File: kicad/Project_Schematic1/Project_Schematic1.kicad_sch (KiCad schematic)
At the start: 40 parts, among them M1 Flag_Servo, M2 Motor_Left, M3 Motor_Bottom, M4 Motor_Right, Q1 NPN, Q2 NPN, Q3 NPN, U1 74xxx244, U2 PIC32MX170F256B, U3 CD4052, U4 QTR-HD-01A, U5 Left_Drum_LEDs, U6 Bottom_Drum_LEDs, U7 Right_Drum_LEDs

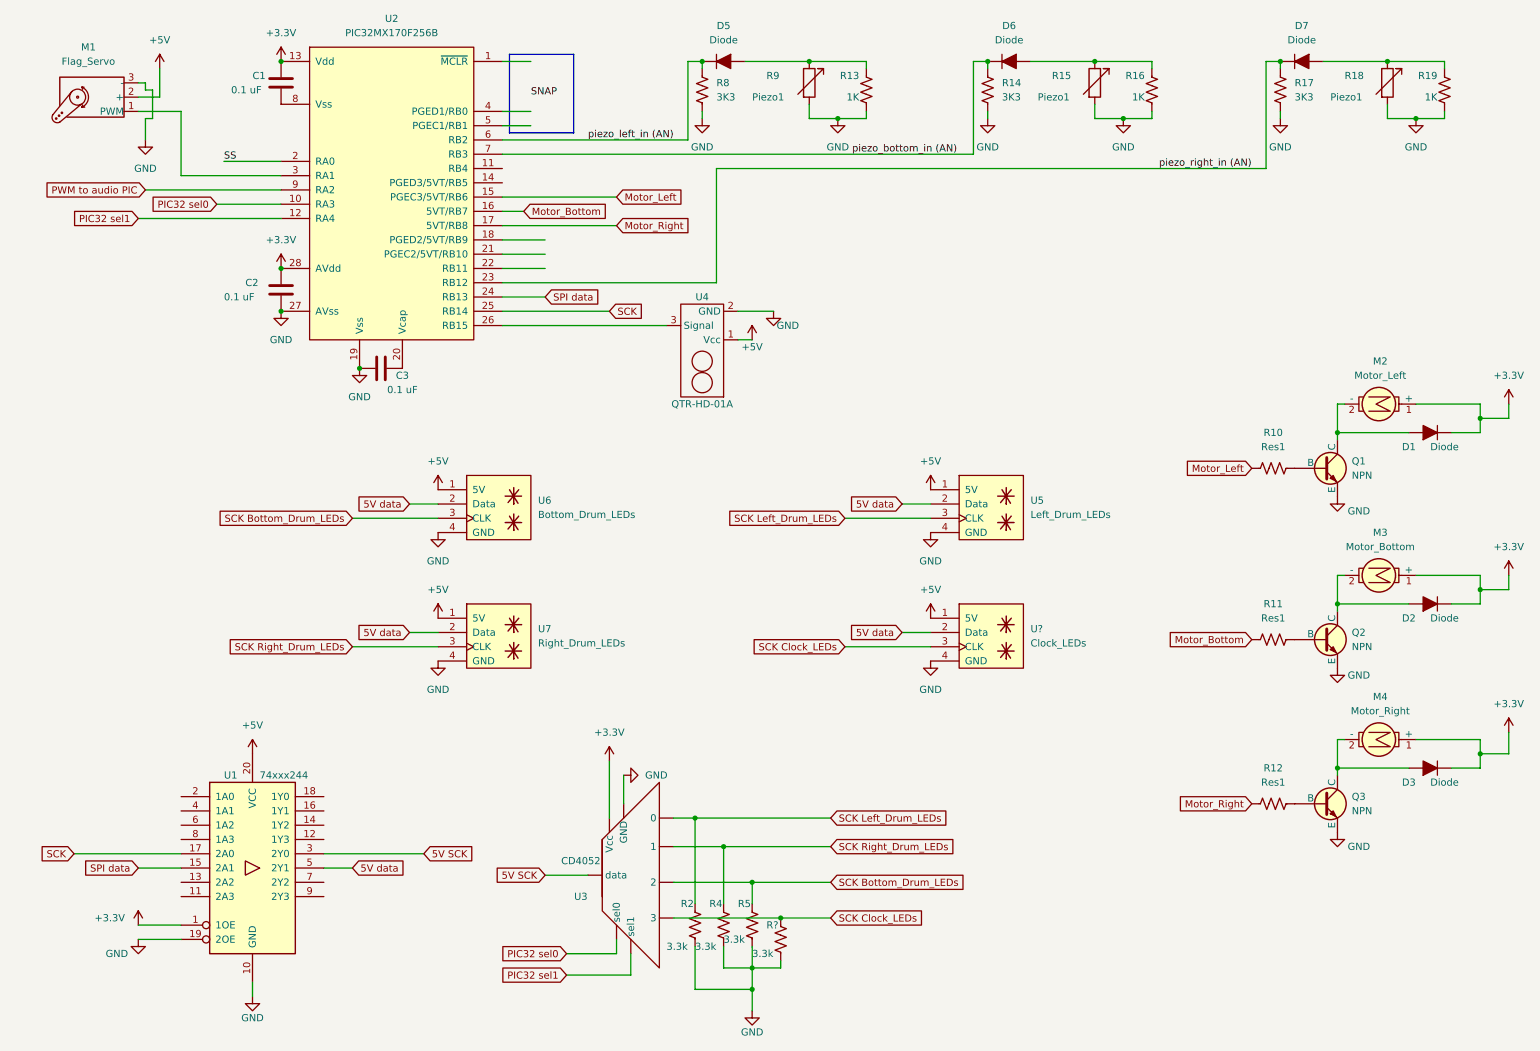
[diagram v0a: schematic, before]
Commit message: Choose custom resistors to constrain piezo voltage below 3.3V
* Rarely exceeds, but especially bottom drum does, so maybe add unity gain buffer
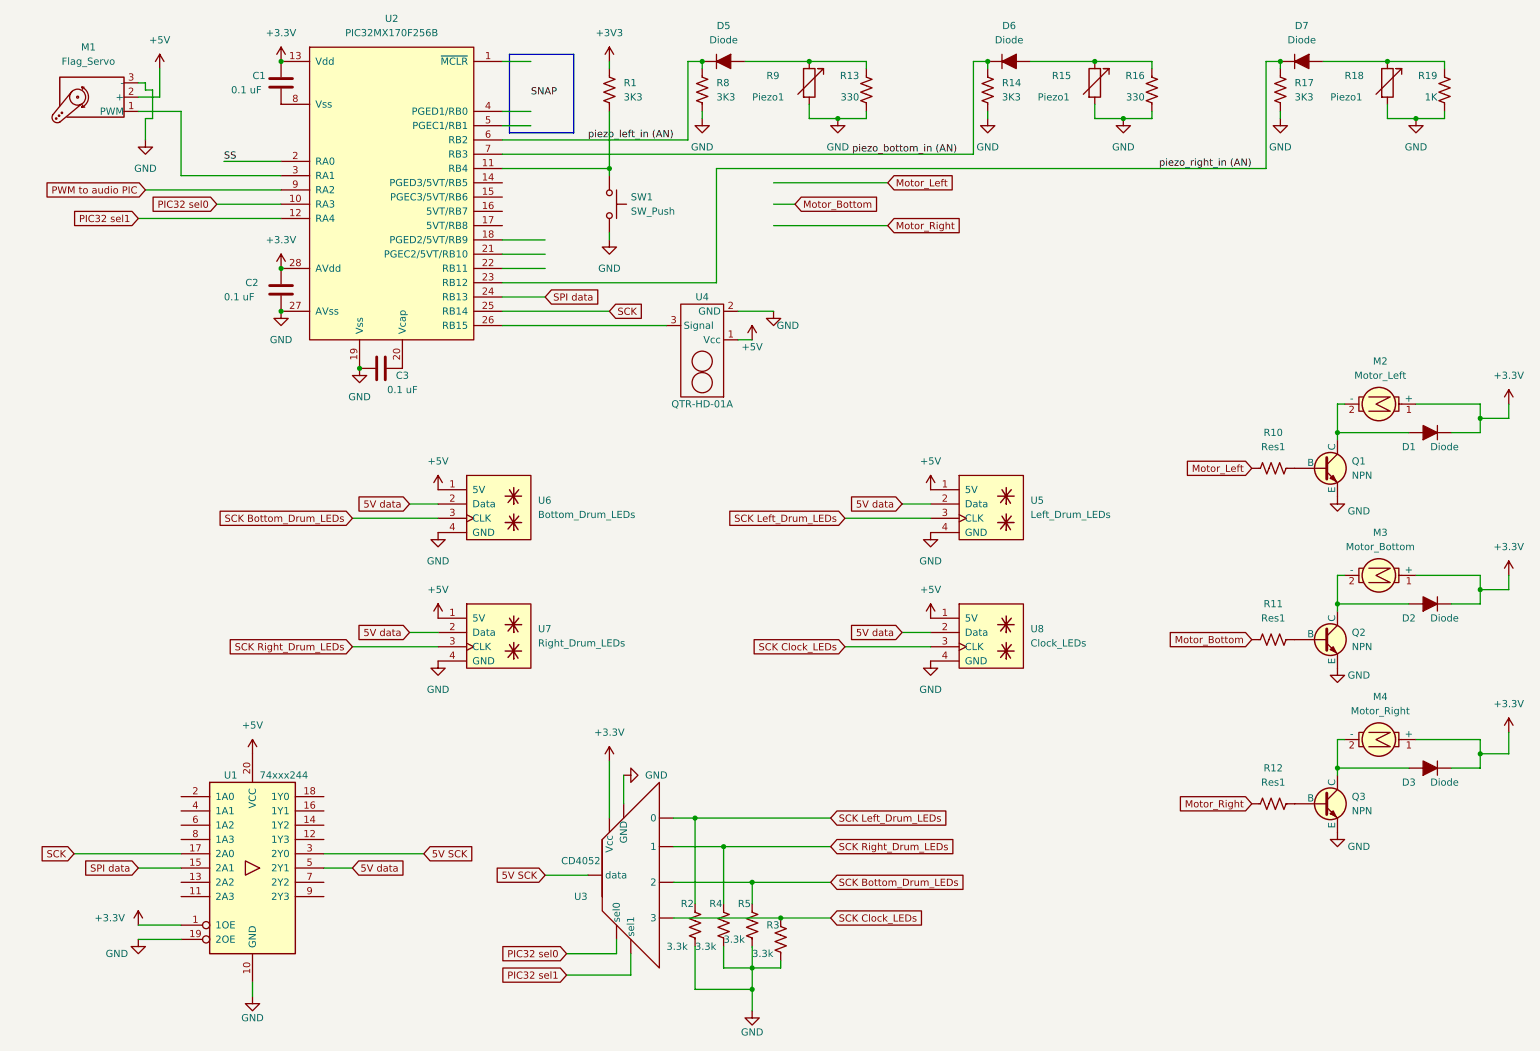
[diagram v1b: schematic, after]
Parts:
- added R1: 3K3, symbol Device:R_US
- added SW1: SW_Push, symbol Switch:SW_Push
- R13, R16: value 1K -> 330
- gave numbers to parts that had none: 2
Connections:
- net GND: now also SW1.2
- net Motor_Bottom: no longer U2.16 (5VT/RB7)
- net Motor_Left: no longer U2.15 (PGEC3/5VT/RB6)
- net Motor_Right: no longer U2.17 (5VT/RB8)
- net at U2.11 (RB4): now also R1.2, SW1.1
- new net +3V3: R1.1

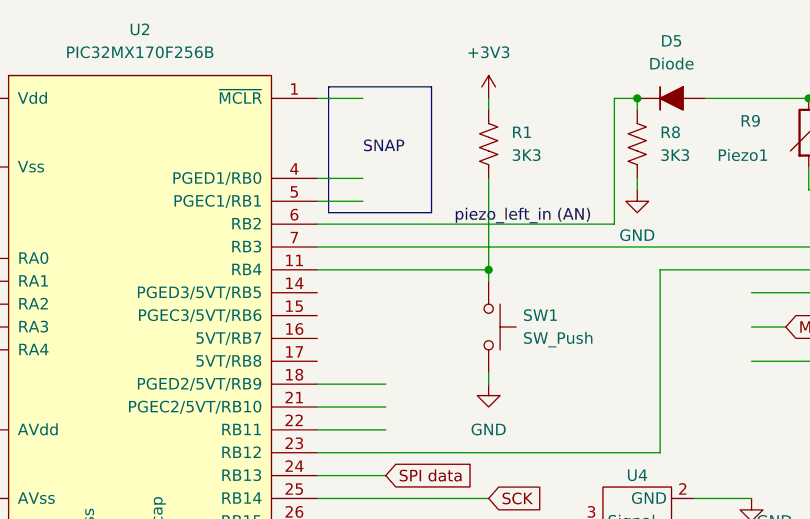
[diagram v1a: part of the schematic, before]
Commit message: Press button to cycle between minimum piezo thresholds
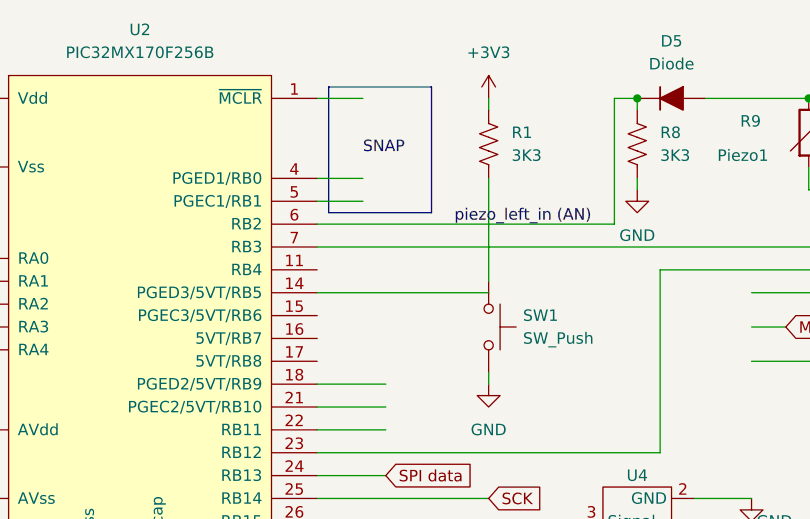
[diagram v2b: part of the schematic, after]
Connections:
- net at R1.2, SW1.1: no longer U2.11 (RB4)
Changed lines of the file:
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@@
   (junction (at 140.97 184.15) (diameter 0) (color 0 0 0 0)
   )
-  (junction (at 115.57 41.91) (diameter 0) (color 0 0 0 0)
-  )
   (junction (at 132.08 22.86) (diameter 0) (color 0 0 0 0)
   )
@@
     (stroke (width 0) (type default) (color 0 0 0 0))
   )
-  (wire (pts (xy 115.57 31.75) (xy 115.57 41.91))
+  (wire (pts (xy 115.57 31.75) (xy 115.57 43.18))
     (stroke (width 0) (type default) (color 0 0 0 0))
   )
@@
     (stroke (width 0) (type default) (color 0 0 0 0))
   )
-  (wire (pts (xy 115.57 41.91) (xy 115.57 43.18))
-    (stroke (width 0) (type default) (color 0 0 0 0))
-  )
   (wire (pts (xy 45.72 48.26) (xy 57.15 48.26))
     (stroke (width 0) (type default) (color 0 0 0 0))
@@
     (stroke (width 0) (type default) (color 0 0 0 0))
   )
+  (wire (pts (xy 96.52 44.45) (xy 115.57 44.45))
+    (stroke (width 0) (type default) (color 0 0 0 0))
+  )
   (wire (pts (xy 182.88 22.86) (xy 182.88 24.13))
     (stroke (width 0) (type default) (color 0 0 0 0))
@@
     (stroke (width 0) (type default) (color 0 0 0 0))
   )
-  (wire (pts (xy 96.52 41.91) (xy 115.57 41.91))
-    (stroke (width 0) (type default) (color 0 0 0 0))
-  )
